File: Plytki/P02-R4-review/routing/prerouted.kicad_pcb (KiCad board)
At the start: 2 copper layers, 160 x 100 mm, 139 parts, among them J1 BAT, J14 PWR, J15 VBAT_IN, J2 VMOTOR, Q1 SUP53P06-20, Q2 SUP53P06-20, Q3 2N5551G, Q4 2N5401YBU, Q5 2N5551G, Q6 2N5551G, Q7 2N5551G, Q8 2N5551G, Q9 SUP53P06-20, U1 LM2936Z-5.0, U10 SN74HC08N, U2 LM2903P, U3 TL431BILP, U4 MCP120-450DI/TO, U5 TSR 2-2450, U6 TSR 2-2433, U7 MCP120-300DI/TO, U8 MCP120-450DI/TO, U9 74LVC125A

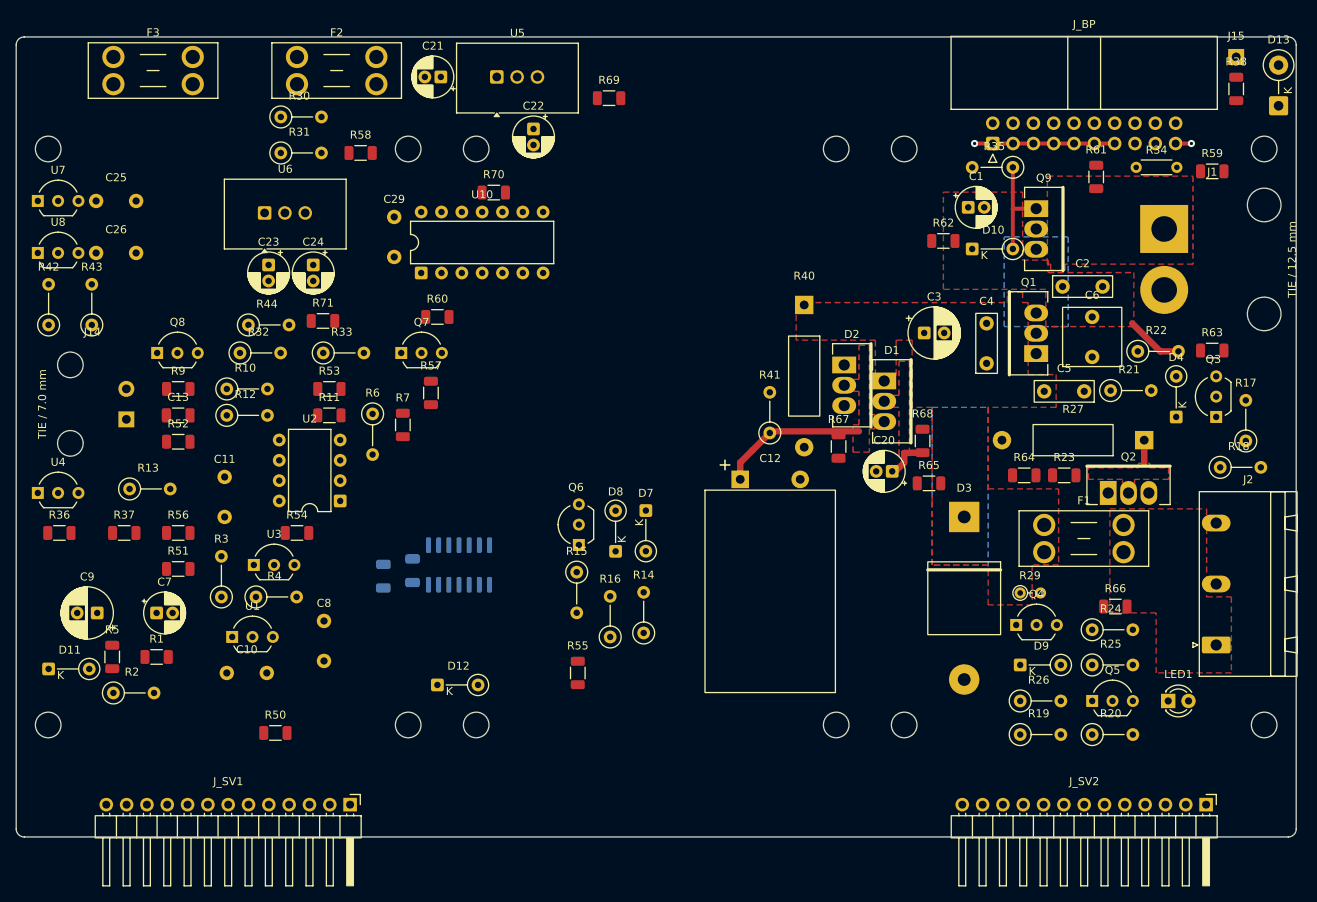
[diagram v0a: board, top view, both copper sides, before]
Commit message: P02 R4 etap 2: rozsunięcie w stronę wolnego pola (wskazanie użytkownika z wydruku 1:1)
Blok sterowania: górna połowa x1,25, dolna x1,12 (układy sztywno z odsprzęganiem i rezystorami
serwisowymi); grupa podtrzymania 8 mm w lewo razem z wylewkami VLOG/HOLD_C i przedłużeniami VSW;
grupa ENABLE 4 mm w lewo; R30, R31, R58, D12 poza strefą H3. Router domknął się w 1. próbie.
DRC bez niepołączeń i innych naruszeń, kontrole PCB 23/23, próby ujemne 12/12, tor 5 A >= 4,1 mm.

Co-Authored-By: Claude Opus 5.5 <noreply@anthropic.com>
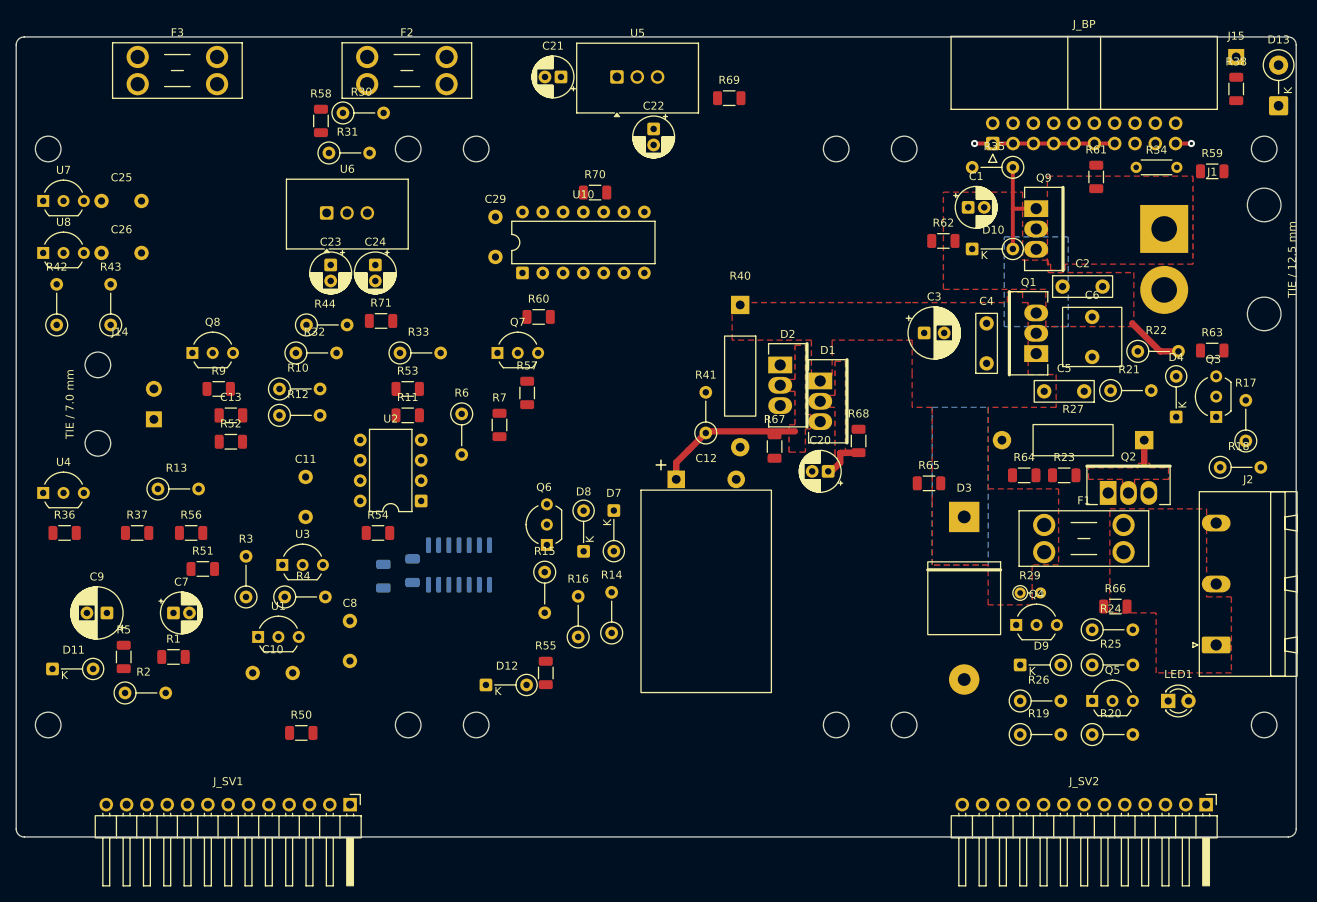
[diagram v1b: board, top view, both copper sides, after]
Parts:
- moved C21 15.0 mm to (68.1, 5.00)
- moved C22 15.0 mm to (79.7, 11.5)
- moved R69 15.0 mm to (89.1, 7.65)
- moved U5 15.0 mm to (75.1, 5.00)
- moved C29 12.7 mm to (59.9, 22.5)
- moved R60 12.7 mm to (65.3, 35.0)
- moved U10 12.7 mm to (63.3, 29.5)
- moved R70 12.7 mm to (72.4, 19.4)
- moved R7 12.1 mm to (60.4, 48.5)
- moved Q7 12.0 mm to (60.2, 39.5)
- moved R57 12.0 mm to (63.9, 44.5)
- moved R6 11.1 mm to (55.7, 47.1)
- moved C11 10.1 mm to (36.2, 60.0)
- moved R54 10.1 mm to (45.2, 62.0)
- moved U2 10.1 mm to (50.6, 58.0)
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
